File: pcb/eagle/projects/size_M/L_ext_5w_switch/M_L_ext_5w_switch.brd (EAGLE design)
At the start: 10 parts

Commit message: PCB M.3
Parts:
- removed L.U1: AT414, atmel:SO14
- added L.R6: 2k2, rcl:R0603
- G.J2: device pinhead2:1X05 -> pinhead2:1X04
- L.R1, L.R2: value (none) -> 1k
- L.R3, L.R4, L.R5: value (none) -> 2k2
- moved L.R1 16.3 mm to (15.9, 17.8), flipped to the top
- moved L.R2 16.3 mm to (13.3, 17.8), flipped to the top, turned to 270 degrees
- moved L.R3 16.2 mm to (10.8, 17.8), flipped to the top, turned to 90 degrees
- moved L.C1 12.5 mm to (17.3, 7.87)
- moved L.R5 6.59 mm to (5.71, 17.8), flipped to the top, turned to 270 degrees
- moved L.R4 5.10 mm to (8.26, 17.8), flipped to the top, turned to 270 degrees
- moved G.J2 1.27 mm to (19.6, 10.5)
- moved L.SW1 0.52 mm to (10.6, 10.7), turned to 0 degrees
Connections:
- removed net N$2: G.J1.2, L.U1.8
- removed net N$3: G.J2.5, L.U1.10
- removed net N$9: L.R1.2, L.SW1.2, L.U1.11
- new net N$4: L.R1.1, L.R2.2, L.SW1.5
- net GND: now also L.R1.2, L.SW1.4; no longer L.SW1.1, L.U1.14
- net N$1: now also L.R4.1, L.R5.1; no longer G.J1.1, L.U1.9
- net N$5: now also L.R2.1, L.R3.2; no longer L.R5.1, L.U1.3
- net N$6: now also L.R3.1, L.R4.2, L.SW1.3; no longer L.R4.1, L.SW1.5, L.U1.2
- net N$7: now also G.J1.5, L.R6.1, L.SW1.1; no longer L.R3.1, L.SW1.4, L.U1.13
- net N$8: now also L.R5.2, L.SW1.2; no longer L.R2.2, L.SW1.3, L.U1.12
- net VCC: now also L.R6.2; no longer L.R1.1, L.R2.1, L.R3.2, L.R4.2, L.R5.2, L.U1.1
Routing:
- net VCC: track 39.7 -> 18.8 mm
- net N$2: track 20.0 -> 0.00 mm, vias 1 -> 0
- net N$1: track 16.9 -> 2.62 mm, vias 1 -> 0
- net N$9: track 10.9 -> 0.00 mm, vias 1 -> 0
- net N$3: track 9.59 -> 0.00 mm
- net N$7: track 7.82 -> 17.4 mm, vias 1 -> 0
- net N$4: track 0.00 -> 9.19 mm
- net GND: track 37.2 -> 45.2 mm, vias 3 -> 2
- net N$8: track 14.2 -> 6.62 mm, vias 1 -> 0
- net N$6: track 9.41 -> 14.2 mm, vias 1 -> 0
- net N$5: track 11.8 -> 15.7 mm, vias 1 -> 0

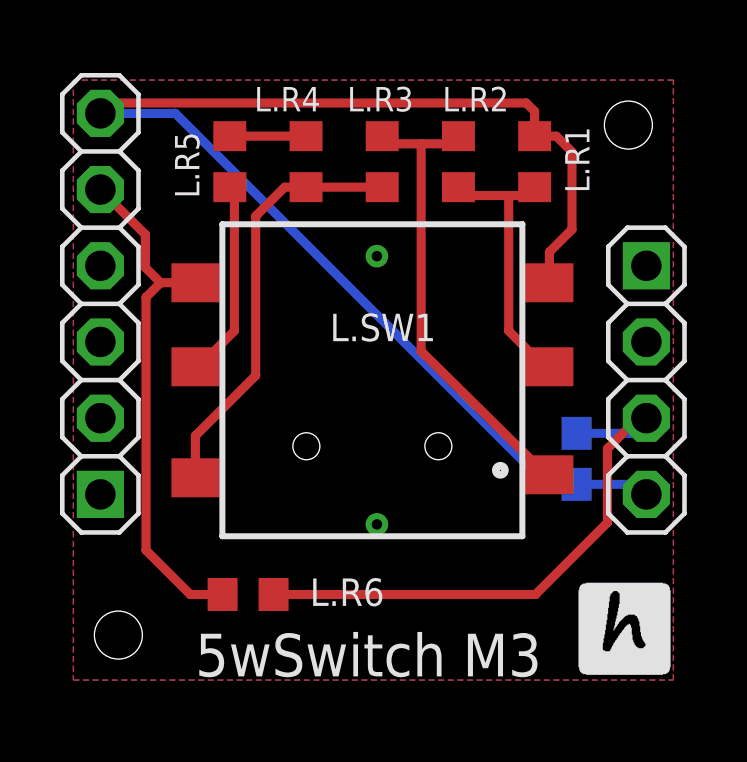
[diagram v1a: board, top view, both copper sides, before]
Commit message: main and switch pcbs adjusted
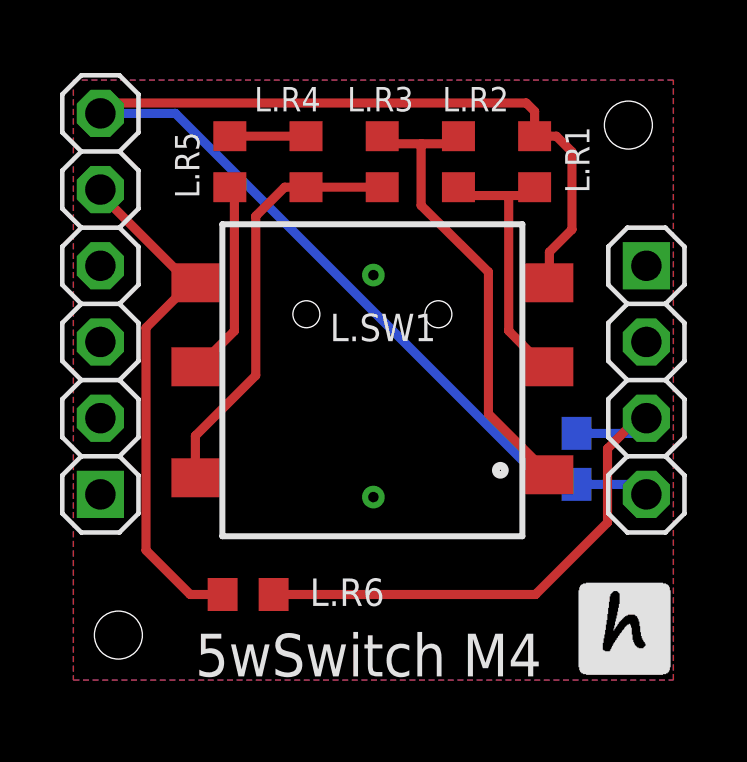
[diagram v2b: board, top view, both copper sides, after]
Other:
- board text added: "5wSwitch M4"
- board text removed: "5wSwitch M3"
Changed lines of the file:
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@@
 <hole x="2" y="2" drill="1.6"/>
 <circle x="2" y="2" radius="1.9" width="0.1" layer="52"/>
-<text x="4.5616" y="0.6222" size="1.4224" layer="21">5wSwitch M3</text>
+<text x="4.5616" y="0.6222" size="1.4224" layer="21">5wSwitch M4</text>
 <hole x="19" y="19" drill="1.6"/>
 <circle x="19" y="19" radius="1.9" width="0.1" layer="52"/>
@@
 <wire x1="15.5956" y1="19.7358" x2="1.7458" y2="19.7358" width="0.3048" layer="1"/>
 <wire x1="1.7458" y1="19.7358" x2="1.4" y2="19.39" width="0.3048" layer="1"/>
-<via x="10.6172" y="14.6304" extent="1-16" drill="0.35"/>
-<via x="10.6172" y="5.6896" extent="1-16" drill="0.35"/>
+<via x="10.5" y="14" extent="1-16" drill="0.35"/>
+<via x="10.5" y="6.6" extent="1-16" drill="0.35"/>
 </signal>
 <signal name="VCC">
@@
 <wire x1="12.0904" y1="18.376" x2="10.922" y2="18.376" width="0.3048" layer="1"/>
 <wire x1="10.922" y1="18.376" x2="10.795" y2="18.63" width="0.3048" layer="1"/>
-<wire x1="12.0904" y1="11.465003125" x2="12.0904" y2="18.376" width="0.3048" layer="1"/>
-<wire x1="16.3664" y1="7.3442" x2="16.26228125" y2="7.3442" width="0.3048" layer="1"/>
-<wire x1="16.26228125" y1="7.3442" x2="12.0904" y2="11.465003125" width="0.3048" layer="1"/>
+<wire x1="12.0904" y1="16.32106875" x2="12.0904" y2="18.376" width="0.3048" layer="1"/>
+<wire x1="14.3344" y1="14.10454375" x2="14.3344" y2="9.3762" width="0.3048" layer="1"/>
+<wire x1="16.3664" y1="7.3442" x2="14.3344" y2="9.3762" width="0.3048" layer="1"/>
+<wire x1="14.3344" y1="14.10454375" x2="12.0904" y2="16.32106875" width="0.3048" layer="1"/>
 </signal>
 <signal name="N$6">
@@
 <contactref element="L.R6" pad="1"/>
 <wire x1="4.572" y1="13.7498" x2="4.5664" y2="13.7442" width="0.3048" layer="1"/>
-<wire x1="4.5664" y1="13.7442" x2="3.4064" y2="13.7442" width="0.3048" layer="1"/>
-<wire x1="2.921" y1="4.826" x2="2.921" y2="13.2588" width="0.3048" layer="1"/>
+<wire x1="4.5664" y1="13.7442" x2="4.3534" y2="13.7442" width="0.3048" layer="1"/>
+<wire x1="2.921" y1="4.826" x2="2.921" y2="12.2428" width="0.3048" layer="1"/>
 <wire x1="4.3942" y1="3.3528" x2="5.4746" y2="3.3528" width="0.3048" layer="1"/>
 <wire x1="2.921" y1="4.826" x2="4.3942" y2="3.3528" width="0.3048" layer="1"/>
-<wire x1="3.4064" y1="13.7442" x2="2.8986" y2="14.252" width="0.3048" layer="1"/>
-<wire x1="2.8986" y1="15.3514" x2="1.4" y2="16.85" width="0.3048" layer="1"/>
-<wire x1="2.8986" y1="14.252" x2="2.8986" y2="15.3514" width="0.3048" layer="1"/>
-<wire x1="2.921" y1="13.2588" x2="3.4064" y2="13.7442" width="0.3048" layer="1"/>
+<wire x1="4.3534" y1="13.7442" x2="1.4" y2="16.6976" width="0.3048" layer="1"/>
+<wire x1="1.4" y1="16.6976" x2="1.4" y2="16.85" width="0.3048" layer="1"/>
+<wire x1="2.921" y1="12.2428" x2="4.397" y2="13.7188" width="0.3048" layer="1"/>
+<wire x1="4.397" y1="13.7188" x2="4.5664" y2="13.7442" width="0" layer="19" extent="1-1"/>
 </signal>
 <signal name="N$1">

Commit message: PCB v7 * 14 pin attiny is main adapter chip now. * changed adapter pin meaning (a1-a5, swapped RX-TX, VUSB replaced by A5, top most pin changed from GND to A4) * changed usb chip of main board
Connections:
- net GND: no longer G.J1.6
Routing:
- net GND: track 45.2 -> 9.61 mm, vias 2 -> 5
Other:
- board text added: "5wSwitch M7"
- board text removed: "5wSwitch M4"
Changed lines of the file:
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@@
 <hole x="2" y="2" drill="1.6"/>
 <circle x="2" y="2" radius="1.9" width="0.1" layer="52"/>
-<text x="4.5616" y="0.6222" size="1.4224" layer="21">5wSwitch M4</text>
+<text x="4.5616" y="0.6222" size="1.4224" layer="21">5wSwitch M7</text>
 <hole x="19" y="19" drill="1.6"/>
 <circle x="19" y="19" radius="1.9" width="0.1" layer="52"/>
@@
 </element>
 <element name="L.R2" library="rcl" library_urn="urn:adsk.eagle:library:334" package="R0603" package3d_urn="urn:adsk.eagle:package:23555/3" value="1k" x="13.335" y="17.78" smashed="yes" rot="R270">
-<attribute name="NAME" x="12.8016" y="19.4564" size="0.8128" layer="25"/>
+<attribute name="NAME" x="14.224" y="18.8976" size="0.8128" layer="25" rot="R270"/>
 <attribute name="POPULARITY" value="70" x="13.335" y="17.78" size="1.778" layer="27" rot="R270" display="off"/>
 <attribute name="SPICEPREFIX" value="R" x="13.335" y="17.78" size="1.778" layer="27" rot="R270" display="off"/>
@@
 </element>
 <element name="L.R1" library="rcl" library_urn="urn:adsk.eagle:library:334" package="R0603" package3d_urn="urn:adsk.eagle:package:23555/3" value="1k" x="15.875" y="17.78" smashed="yes" rot="R90">
-<attribute name="NAME" x="16.891" y="18.9484" size="0.8128" layer="25" rot="R270"/>
+<attribute name="NAME" x="16.7386" y="18.923" size="0.8128" layer="25" rot="R270"/>
 <attribute name="POPULARITY" value="70" x="15.875" y="17.78" size="1.778" layer="27" rot="R90" display="off"/>
 <attribute name="SPICEPREFIX" value="R" x="15.875" y="17.78" size="1.778" layer="27" rot="R90" display="off"/>
@@
 </element>
 <element name="L.R3" library="rcl" library_urn="urn:adsk.eagle:library:334" package="R0603" package3d_urn="urn:adsk.eagle:package:23555/3" value="2k2" x="10.795" y="17.78" smashed="yes" rot="R90">
-<attribute name="NAME" x="9.6266" y="19.4564" size="0.8128" layer="25"/>
+<attribute name="NAME" x="11.6078" y="18.8722" size="0.8128" layer="25" rot="R270"/>
 <attribute name="POPULARITY" value="70" x="10.795" y="17.78" size="1.778" layer="27" rot="R90" display="off"/>
 <attribute name="SPICEPREFIX" value="R" x="10.795" y="17.78" size="1.778" layer="27" rot="R90" display="off"/>
@@
 </element>
 <element name="L.R4" library="rcl" library_urn="urn:adsk.eagle:library:334" package="R0603" package3d_urn="urn:adsk.eagle:package:23555/3" value="2k2" x="8.255" y="17.78" smashed="yes" rot="R270">
-<attribute name="NAME" x="6.5278" y="19.4564" size="0.8128" layer="25"/>
+<attribute name="NAME" x="9.0678" y="18.8722" size="0.8128" layer="25" rot="R270"/>
 <attribute name="POPULARITY" value="70" x="8.255" y="17.78" size="1.778" layer="27" rot="R270" display="off"/>
 <attribute name="SPICEPREFIX" value="R" x="8.255" y="17.78" size="1.778" layer="27" rot="R270" display="off"/>
@@
 </element>
 <element name="L.R5" library="rcl" library_urn="urn:adsk.eagle:library:334" package="R0603" package3d_urn="urn:adsk.eagle:package:23555/3" value="2k2" x="5.715" y="17.78" smashed="yes" rot="R270">
-<attribute name="NAME" x="4.699" y="16.5608" size="0.8128" layer="25" rot="R90"/>
+<attribute name="NAME" x="6.5532" y="18.923" size="0.8128" layer="25" rot="R270"/>
 <attribute name="POPULARITY" value="70" x="5.715" y="17.78" size="1.778" layer="27" rot="R270" display="off"/>
 <attribute name="SPICEPREFIX" value="R" x="5.715" y="17.78" size="1.778" layer="27" rot="R270" display="off"/>
@@
 </element>
 <element name="L.R6" library="rcl" library_urn="urn:adsk.eagle:library:334" package="R0603" package3d_urn="urn:adsk.eagle:package:23555/3" value="2k2" x="6.3246" y="3.3528" smashed="yes">
-<attribute name="NAME" x="8.382" y="2.9718" size="0.9144" layer="25"/>
+<attribute name="NAME" x="5.0546" y="4.0894" size="0.8128" layer="25"/>
 <attribute name="POPULARITY" value="70" x="6.3246" y="3.3528" size="1.778" layer="27" display="off"/>
 <attribute name="SPICEPREFIX" value="R" x="6.3246" y="3.3528" size="1.778" layer="27" display="off"/>
@@
 <signals>
 <signal name="GND">
-<polygon width="0.3048" layer="1" isolate="0.3048">
+<polygon width="0.254" layer="1" isolate="0.254">
 <vertex x="0.5" y="20.5"/>
 <vertex x="0.5" y="0.5"/>
@@
 </polygon>
 <contactref element="L.C1" pad="1"/>
-<polygon width="0.3048" layer="16" isolate="0.3048">
+<polygon width="0.254" layer="16" isolate="0.254">
 <vertex x="0.5" y="20.5"/>
 <vertex x="0.5" y="0.5"/>
@@
 </polygon>
 <contactref element="G.J2" pad="4"/>
-<contactref element="G.J1" pad="6"/>
 <contactref element="L.R1" pad="2"/>
 <contactref element="L.SW1" pad="4"/>
@@
 <wire x1="19.266" y1="7.024" x2="17.272" y2="7.024" width="0.3048" layer="16"/>
 <wire x1="17.272" y1="7.024" x2="16.26714375" y2="7.024" width="0.3048" layer="16"/>
-<wire x1="16.26714375" y1="7.024" x2="3.90114375" y2="19.39" width="0.3048" layer="16"/>
-<wire x1="3.90114375" y1="19.39" x2="1.4" y2="19.39" width="0.3048" layer="16"/>
 <wire x1="16.3664" y1="14.7662" x2="17.1196" y2="15.5194" width="0.3048" layer="1"/>
 <wire x1="17.1196" y1="15.5194" x2="17.1196" y2="18.1102" width="0.3048" layer="1"/>
 <wire x1="17.1196" y1="18.1102" x2="16.5998" y2="18.63" width="0.3048" layer="1"/>
 <wire x1="16.5998" y1="18.63" x2="15.875" y2="18.63" width="0.3048" layer="1"/>
-<wire x1="15.875" y1="18.63" x2="15.875" y2="19.4564" width="0.3048" layer="1"/>
-<wire x1="15.875" y1="19.4564" x2="15.5956" y2="19.7358" width="0.3048" layer="1"/>
-<wire x1="15.5956" y1="19.7358" x2="1.7458" y2="19.7358" width="0.3048" layer="1"/>
-<wire x1="1.7458" y1="19.7358" x2="1.4" y2="19.39" width="0.3048" layer="1"/>
 <via x="10.5" y="14" extent="1-16" drill="0.35"/>
 <via x="10.5" y="6.6" extent="1-16" drill="0.35"/>
+<via x="3.4798" y="19.939" extent="1-16" drill="0.35"/>
+<via x="16.7132" y="19.9644" extent="1-16" drill="0.35"/>
+<via x="1.524" y="4.4958" extent="1-16" drill="0.35"/>
 </signal>
 <signal name="VCC">
